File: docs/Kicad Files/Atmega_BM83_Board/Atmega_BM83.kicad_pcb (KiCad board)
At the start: 2 copper layers, 114.3 x 88.9 mm, 35 parts, among them J1 18V, J10 ICE Header, J2 Out to Amp, J3 PWR SW, J4 Volume POT, J5 Pairing BTN, J6 PWR LED, J7 Pair LED, J8 Conn_01x12, J9 Conn_01x12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

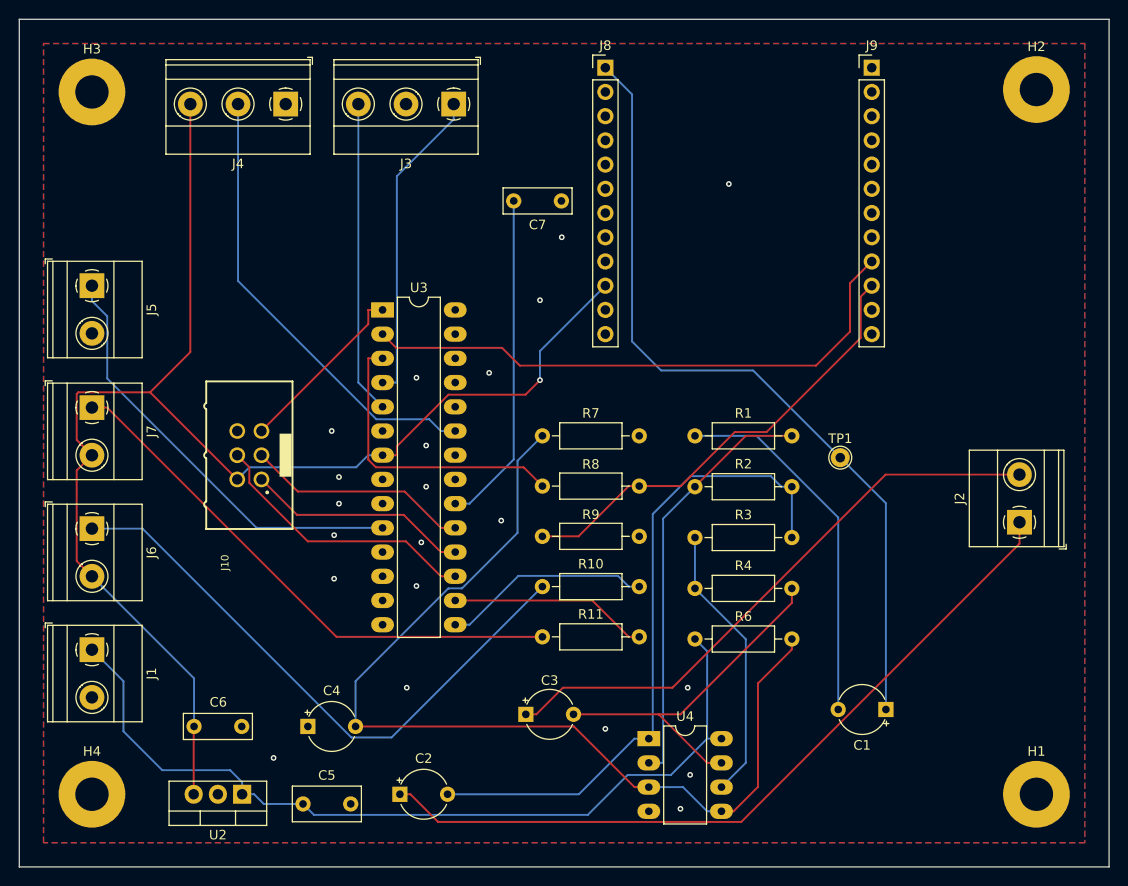
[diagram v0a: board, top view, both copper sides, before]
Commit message: BT/MC PCB redesign. rerouted traces. awaiting QA inspection
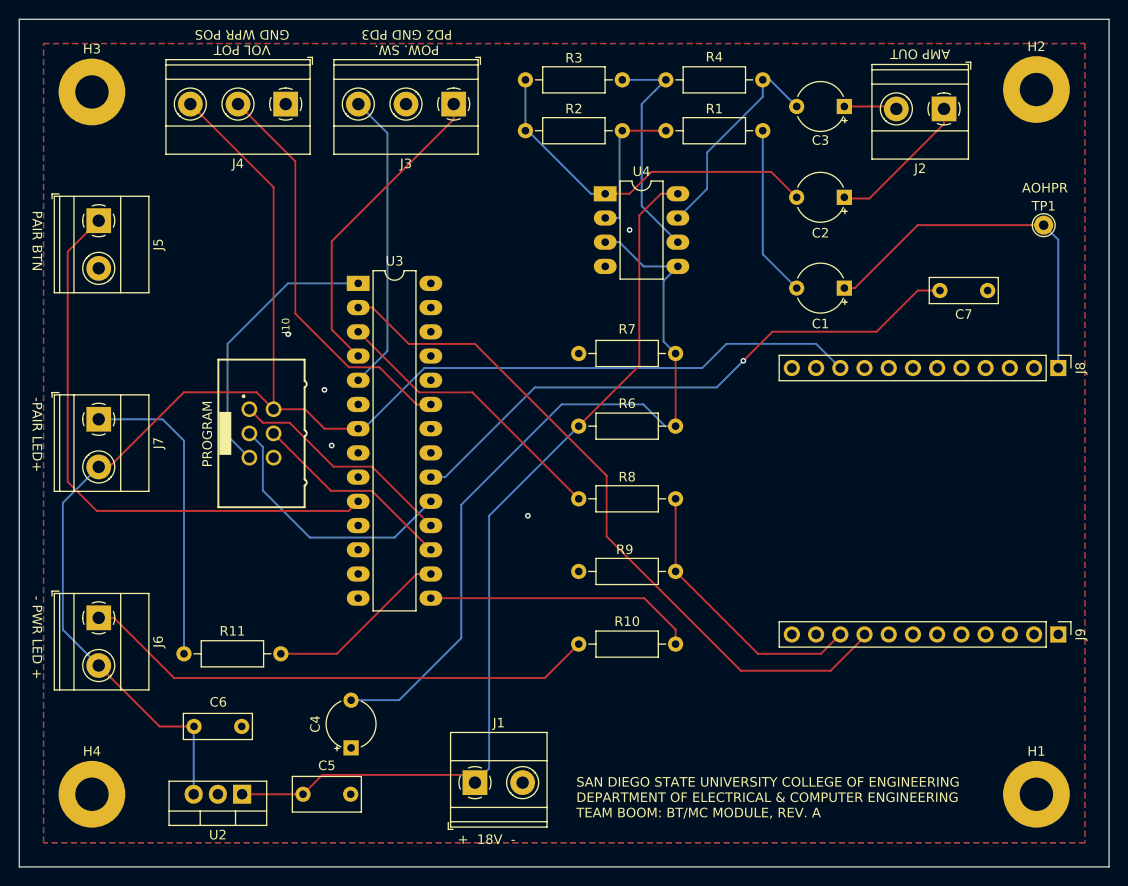
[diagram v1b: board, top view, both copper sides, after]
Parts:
- moved C2 78.1 mm to (137.3, 82.2), turned to 180 degrees
- moved C3 72.0 mm to (137.3, 72.6), turned to 180 degrees
- moved J9 62.6 mm to (159.8, 128.0), turned to -90 degrees
- moved U4 57.3 mm to (112.3, 81.8)
- moved J8 57.0 mm to (159.8, 100.1), turned to -90 degrees
- moved R4 53.4 mm to (118.6, 69.8)
- moved R3 48.6 mm to (114.0, 69.8), turned to 180 degrees
- moved C7 45.7 mm to (152.4, 91.9)
- moved C1 44.4 mm to (137.3, 91.7)
- moved J2 44.1 mm to (147.8, 72.9), turned to 180 degrees
- moved J1 42.5 mm to (98.6, 143.6), turned to 0 degrees
- moved R2 38.1 mm to (114.0, 75.2), turned to 180 degrees
- moved R11 37.6 mm to (68.1, 130.0)
- moved R1 32.8 mm to (128.8, 75.2), turned to 180 degrees
- moved TP1 32.4 mm to (158.2, 85.1)
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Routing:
- net Net-(J2-Pin_1): track 80.5 -> 15.3 mm
- net Net-(J2-Pin_2): track 62.2 -> 5.56 mm
- net AOHPR: track 85.2 -> 39.3 mm
- net Net-(C2-Pad2): track 69.3 -> 38.6 mm
- net Net-(U4A--): track 44.2 -> 15.3 mm
- net Net-(U3-AVCC): track 35.2 -> 61.5 mm, vias 0 -> 1
- net Net-(J7-Pin_1): track 57.2 -> 32.2 mm
- net 8V: track 103.4 -> 82.6 mm
- net Net-(C1-Pad2): track 38.7 -> 18.0 mm
- net BM83 Rx: track 48.0 -> 29.3 mm
- net 5V: track 150.5 -> 166.7 mm, vias 1 -> 0
- net Net-(J5-Pin_1): track 45.8 -> 60.9 mm
- net Net-(C3-Pad2): track 38.0 -> 23.4 mm
- net BM83 Tx: track 60.2 -> 74.3 mm
- net /RESET: track 18.8 -> 29.2 mm
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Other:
- board text added: "+ 18V -"
- board text added: "- PWR LED +"
- board text added: "-PAIR LED+"
- board text added: "AMP OUT"
- board text added: "AOHPR"
- board text added: "PAIR BTN"
- board text added: "POW. SW. PD2 GND PD3"
- board text added: "PROGRAM"
- board text added: "SAN DIEGO STATE UNIVERSITY COLLEGE OF ENGINEERING DEPARTMENT OF ELECTRICAL & COMPUTER ENGINEERING TEAM BOOM: BT/MC MODULE, REV. A"
- board text added: "VOL POT GND WPR POS"

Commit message: final changes to both PCBs before review
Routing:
- net GND: vias 5 -> 8
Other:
- board text added: "BM83 Module"
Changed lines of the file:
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@@
+		)
+	)
+	(gr_text "BM83 Module"
+		(at 144.5 110.1 -90)
+		(layer "F.SilkS")
+		(effects
+			(font
+				(size 1 1)
+				(thickness 0.15)
+			)
+			(justify left bottom)
 		)
 	)
@@
 	)
 	(via
+		(at 89.9 113.8)
+		(size 0.6)
+		(drill 0.3)
+		(layers "F.Cu" "B.Cu")
+		(free yes)
+		(net 7)
+	)
+	(via
 		(at 104.14 115.57)
 		(size 0.6)
@@
 		(net 7)
 	)
+	(via
+		(at 91 98.6)
+		(size 0.6)
+		(drill 0.3)
+		(layers "F.Cu" "B.Cu")
+		(free yes)
+		(net 7)
+	)
+	(via
+		(at 83.3 111.2)
+		(size 0.6)
+		(drill 0.3)
+		(layers "F.Cu" "B.Cu")
+		(free yes)
+		(net 7)
+	)
 	(segment
 		(start 119.634 106.172)
@@
 		(polygon
 			(pts
-				(xy 53.34 66.04) (xy 162.56 66.04) (xy 162.56 149.86) (xy 53.34 149.86)
+				(xy 51.3 64) (xy 164.6 64) (xy 164.6 151.9) (xy 51.3 151.9)
 			)
 		)
@@
 		(layer "B.Cu")
 		(hatch edge 0.5)
-		(priority 1)
 		(connect_pads
 			(clearance 0.5)
@@
 		(polygon
 			(pts
-				(xy 53.34 66.04) (xy 162.56 66.04) (xy 162.56 149.86) (xy 53.34 149.86)
+				(xy 51.3 64) (xy 164.6 64) (xy 164.6 151.9) (xy 51.3 151.9)
 			)
 		)
